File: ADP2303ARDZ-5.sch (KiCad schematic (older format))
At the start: 11 parts

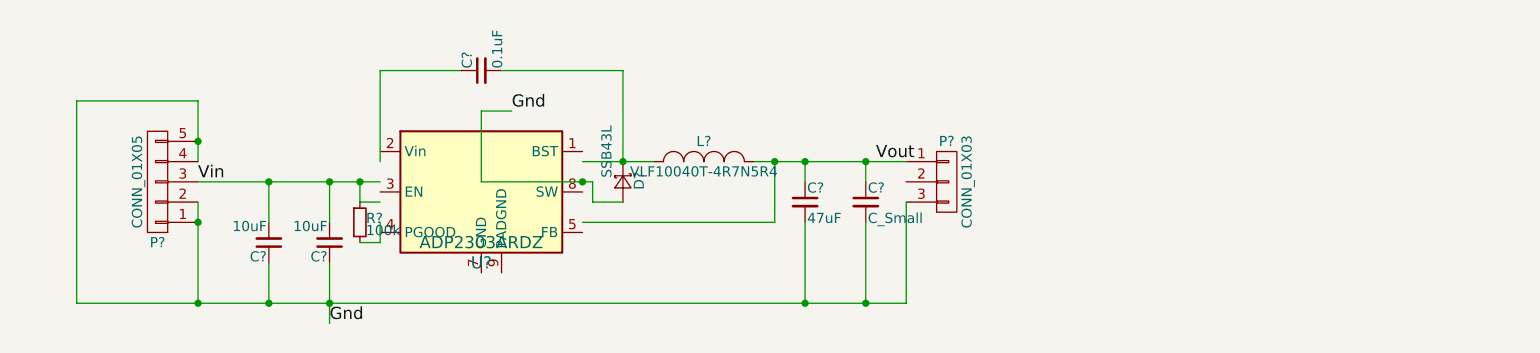
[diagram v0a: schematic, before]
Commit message: Created the board file but not laid out as yet.
Signed-off-by: John Whitmore <johnfwhitmore@gmail.com>
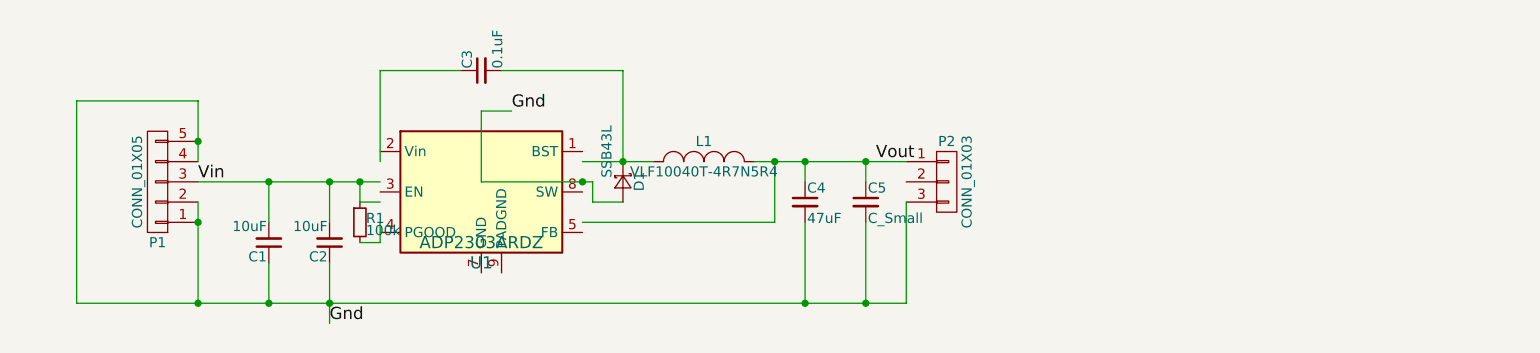
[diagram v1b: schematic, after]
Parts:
- C1, C2, C3, C4, C5: renamed from C?; footprint (none) -> Capacitors_SMD:C_0603_HandSoldering
- D1: renamed from D?; footprint (none) -> Diodes_SMD:DO-214AB_Handsoldering
- L1: renamed from L?; footprint (none) -> electronicSoup:VLF10040_Inductor
- P1: renamed from P?; footprint (none) -> Pin_Headers:Pin_Header_Straight_1x05
- P2: renamed from P?; footprint (none) -> Pin_Headers:Pin_Header_Straight_1x03
- R1: renamed from R?; footprint (none) -> Resistors_SMD:R_0603_HandSoldering
- U1: renamed from U?; footprint (none) -> SMD_Packages:SOIC-8-N
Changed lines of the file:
@@
 $EndDescr
 $Comp
-L ADP2303ARDZ U?
+L ADP2303ARDZ U1
 U 1 1 59F0DD7C
 P 5700 3600
-F 0 "U?" H 5700 3250 60  0000 C CNN
+F 0 "U1" H 5700 3250 60  0000 C CNN
 F 1 "ADP2303ARDZ" H 5700 3350 60  0000 C CNN
-F 2 "" H 5700 3600 60  0000 C CNN
+F 2 "SMD_Packages:SOIC-8-N" H 5700 3600 60  0001 C CNN
 F 3 "" H 5700 3600 60  0000 C CNN
 	1    5700 3600
@@
 $EndComp
 $Comp
-L C_Small C?
+L C_Small C2
 U 1 1 59F0DDA1
 P 4950 3850
-F 0 "C?" H 4960 3920 50  0000 L CNN
+F 0 "C2" H 4960 3920 50  0000 L CNN
 F 1 "10uF" H 4960 3770 50  0000 L CNN
-F 2 "" H 4950 3850 50  0000 C CNN
+F 2 "Capacitors_SMD:C_0603_HandSoldering" H 4950 3850 50  0001 C CNN
 F 3 "" H 4950 3850 50  0000 C CNN
 	1    4950 3850
@@
 $EndComp
 $Comp
-L C_Small C?
+L C_Small C4
 U 1 1 59F0DE2E
 P 7300 3650
-F 0 "C?" H 7310 3720 50  0000 L CNN
+F 0 "C4" H 7310 3720 50  0000 L CNN
 F 1 "47uF" H 7310 3570 50  0000 L CNN
-F 2 "" H 7300 3650 50  0000 C CNN
+F 2 "Capacitors_SMD:C_0603_HandSoldering" H 7300 3650 50  0001 C CNN
 F 3 "" H 7300 3650 50  0000 C CNN
 	1    7300 3650
@@
 $EndComp
 $Comp
-L C_Small C?
+L C_Small C3
 U 1 1 59F0DF1E
 P 5700 3000
-F 0 "C?" H 5710 3070 50  0000 L CNN
+F 0 "C3" H 5710 3070 50  0000 L CNN
 F 1 "0.1uF" H 5710 2920 50  0000 L CNN
-F 2 "" H 5700 3000 50  0000 C CNN
+F 2 "Capacitors_SMD:C_0603_HandSoldering" H 5700 3000 50  0001 C CNN
 F 3 "" H 5700 3000 50  0000 C CNN
 	1    5700 3000
@@
 Gnd
 $Comp
-L D_Schottky_Small D?
+L D_Schottky_Small D1
 U 1 1 59F0DF9A
 P 6400 3550
-F 0 "D?" H 6350 3630 50  0000 L CNN
+F 0 "D1" H 6350 3630 50  0000 L CNN
 F 1 "SSB43L" H 6120 3470 50  0000 L CNN
-F 2 "" V 6400 3550 50  0000 C CNN
+F 2 "Diodes_SMD:DO-214AB_Handsoldering" V 6400 3550 50  0001 C CNN
 F 3 "" V 6400 3550 50  0000 C CNN
 	1    6400 3550
@@
 	6200 3450 6550 3450
 $Comp
-L INDUCTOR_SMALL L?
+L INDUCTOR_SMALL L1
 U 1 1 59F0E044
 P 6800 3450
-F 0 "L?" H 6800 3550 50  0000 C CNN
+F 0 "L1" H 6800 3550 50  0000 C CNN
 F 1 "VLF10040T-4R7N5R4" H 6800 3400 50  0000 C CNN
-F 2 "" H 6800 3450 50  0000 C CNN
+F 2 "electronicSoup:VLF10040_Inductor" H 6800 3450 50  0001 C CNN
 F 3 "" H 6800 3450 50  0000 C CNN
 	1    6800 3450
@@
 Vout
 $Comp
-L CONN_01X05 P?
+L CONN_01X05 P1
 U 1 1 59F0E19C
 P 4100 3550
-F 0 "P?" H 4100 3850 50  0000 C CNN
+F 0 "P1" H 4100 3850 50  0000 C CNN
 F 1 "CONN_01X05" V 4200 3550 50  0000 C CNN
-F 2 "" H 4100 3550 50  0000 C CNN
+F 2 "Pin_Headers:Pin_Header_Straight_1x05" H 4100 3550 50  0001 C CNN
 F 3 "" H 4100 3550 50  0000 C CNN
 	1    4100 3550
@@
 Connection ~ 4300 3350
 $Comp
-L CONN_01X03 P?
+L CONN_01X03 P2
 U 1 1 59F0E2CF
 P 8000 3550
-F 0 "P?" H 8000 3750 50  0000 C CNN
+F 0 "P2" H 8000 3750 50  0000 C CNN
 F 1 "CONN_01X03" V 8100 3550 50  0000 C CNN
-F 2 "" H 8000 3550 50  0000 C CNN
+F 2 "Pin_Headers:Pin_Header_Straight_1x03" H 8000 3550 50  0001 C CNN
 F 3 "" H 8000 3550 50  0000 C CNN
 	1    8000 3550
@@
 Connection ~ 7300 4150
 $Comp
-L R_Small R?
+L R_Small R1
 U 1 1 59F0E3EF
 P 5100 3750
-F 0 "R?" H 5130 3770 50  0000 L CNN
+F 0 "R1" H 5130 3770 50  0000 L CNN
 F 1 "100k" H 5130 3710 50  0000 L CNN
-F 2 "" H 5100 3750 50  0000 C CNN
+F 2 "Resistors_SMD:R_0603_HandSoldering" H 5100 3750 50  0001 C CNN
 F 3 "" H 5100 3750 50  0000 C CNN
 	1    5100 3750
@@
 	5200 3850 5200 3750
 $Comp
-L C_Small C?
+L C_Small C5
 U 1 1 59F0E60C
 P 7600 3650
-F 0 "C?" H 7610 3720 50  0000 L CNN
+F 0 "C5" H 7610 3720 50  0000 L CNN
 F 1 "C_Small" H 7610 3570 50  0000 L CNN
-F 2 "" H 7600 3650 50  0000 C CNN
+F 2 "Capacitors_SMD:C_0603_HandSoldering" H 7600 3650 50  0001 C CNN
 F 3 "" H 7600 3650 50  0000 C CNN
 	1    7600 3650
@@
 Connection ~ 4950 3550
 $Comp
-L C_Small C?
+L C_Small C1
 U 1 1 59F0E819
 P 4650 3850
-F 0 "C?" H 4660 3920 50  0000 L CNN
+F 0 "C1" H 4660 3920 50  0000 L CNN
 F 1 "10uF" H 4660 3770 50  0000 L CNN
-F 2 "" H 4650 3850 50  0000 C CNN
+F 2 "Capacitors_SMD:C_0603_HandSoldering" H 4650 3850 50  0001 C CNN
 F 3 "" H 4650 3850 50  0000 C CNN
 	1    4650 3850

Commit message: Added the dc-dc converters to the official kicad library
Forked the kicad-libraries github project and added the ADP230x and MCP1825s and used both components in this design
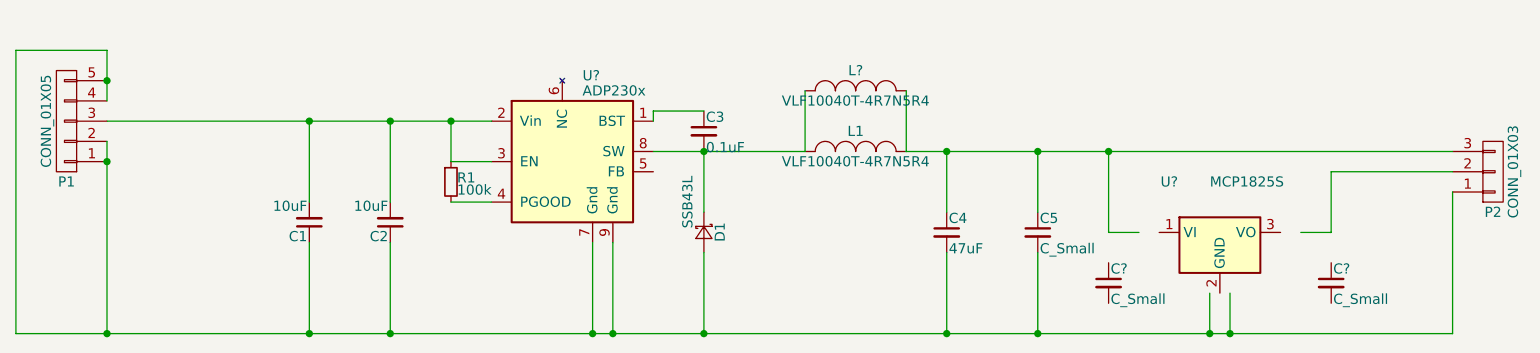
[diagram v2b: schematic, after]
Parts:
- removed U1: ADP2303ARDZ, SMD_Packages:SOIC-8-N, symbol ADP2303ARDZ
- added C? (x2): C_Small, Capacitors_SMD:C_0603_HandSoldering, symbol C_Small
- added L?: VLF10040T-4R7N5R4, electronicSoup:VLF10040_Inductor, symbol INDUCTOR_SMALL
- added U?: ADP230x, Housings_SOIC:SOIC-8-1EP_3.9x4.9mm_Pitch1.27mm, symbol ADP230x
- added U?: MCP1825S, TO_SOT_Packages_SMD:SOT-223, symbol MCP1825S
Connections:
- net labels removed: Gnd, Vin, Vout
- wire segments 32 -> 35
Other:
- moved on the sheet: C1, C2, C3, C4, C5, D1, L1, P1, P2, R1

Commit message: moved to v5 footprints so a few missing
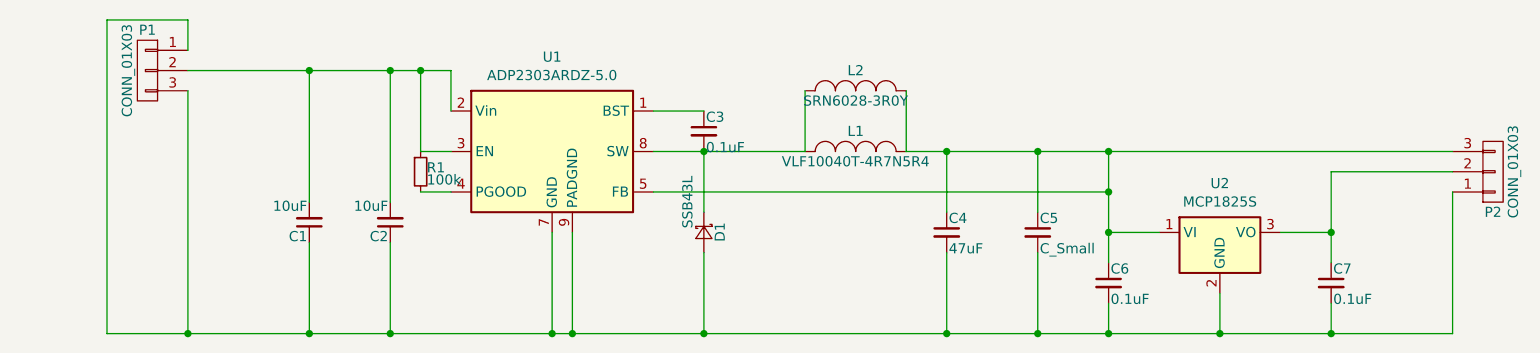
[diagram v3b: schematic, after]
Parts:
- removed P1: CONN_01X05, Pin_Headers:Pin_Header_Straight_1x05, symbol CONN_01X05
- removed U?: ADP230x, Housings_SOIC:SOIC-8-1EP_3.9x4.9mm_Pitch1.27mm, symbol ADP230x
- removed U?: MCP1825S, TO_SOT_Packages_SMD:SOT-223, symbol MCP1825S
- added P1: CONN_01X03, Conn_PinSocket_2.54mm:PinSocket_1x03_P2.54mm_Vertical, symbol CONN_01X03
- added U1: ADP2303ARDZ-5.0, Housings_SOIC:SOIC-8-1EP_3.9x4.9mm_Pitch1.27mm, symbol ADP2303ARDZ-5.0
- added U2: MCP1825S, symbol MCP1825S
- C1, C2, C3, C4, C5: footprint Capacitors_SMD:C_0603_HandSoldering -> Capacitor_SMD:C_0603_1608Metric_Pad0.84x1.00mm_HandSolder
- C6, C7: renamed from C?; value C_Small -> 0.1uF; footprint Capacitors_SMD:C_0603_HandSoldering -> Capacitor_SMD:C_0603_1608Metric_Pad0.84x1.00mm_HandSolder
- D1: footprint Diodes_SMD:DO-214AB_Handsoldering -> Diode_SMD:D_SMB_Handsoldering
- L1: footprint electronicSoup:VLF10040_Inductor -> Inductor_SMD:L_TDK_VLF10040
- L2: renamed from L?; value VLF10040T-4R7N5R4 -> SRN6028-3R0Y; footprint electronicSoup:VLF10040_Inductor -> Inductor_SMD:L_Bourns-SRN6028
- P2: footprint Pin_Headers:Pin_Header_Straight_1x03 -> Conn_PinSocket_2.54mm:PinSocket_1x03_P2.54mm_Vertical
- R1: footprint Resistors_SMD:R_0603_HandSoldering -> Resistor_SMD:R_0603_1608Metric_Pad0.84x1.00mm_HandSolder
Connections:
- wire segments 35 -> 37
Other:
- moved on the sheet: R1
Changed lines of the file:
@@
-EESchema Schematic File Version 2
+EESchema Schematic File Version 3
+LIBS:ADP2303ARDZ-5-rescue
 LIBS:ac-dc
 LIBS:adc-dac
@@
 LIBS:Zilog
 LIBS:ADP2303ARDZ-5-cache
-EELAYER 25 0
+EELAYER 26 0
 EELAYER END
 $Descr A4 11693 8268
@@
 F 0 "C2" H 5260 3820 50  0000 L CNN
 F 1 "10uF" H 5260 3670 50  0000 L CNN
-F 2 "Capacitors_SMD:C_0603_HandSoldering" H 5250 3750 50  0001 C CNN
+F 2 "Capacitor_SMD:C_0603_1608Metric_Pad0.84x1.00mm_HandSolder" H 5250 3750 50  0001 C CNN
 F 3 "" H 5250 3750 50  0000 C CNN
 	1    5250 3750
@@
 F 0 "C4" H 8010 3870 50  0000 L CNN
 F 1 "47uF" H 8010 3720 50  0000 L CNN
-F 2 "Capacitors_SMD:C_0603_HandSoldering" H 8000 3800 50  0001 C CNN
+F 2 "Capacitor_SMD:C_0603_1608Metric_Pad0.84x1.00mm_HandSolder" H 8000 3800 50  0001 C CNN
 F 3 "" H 8000 3800 50  0000 C CNN
 	1    8000 3800
@@
 F 0 "C3" H 6810 3370 50  0000 L CNN
 F 1 "0.1uF" H 6810 3220 50  0000 L CNN
-F 2 "Capacitors_SMD:C_0603_HandSoldering" H 6800 3300 50  0001 C CNN
+F 2 "Capacitor_SMD:C_0603_1608Metric_Pad0.84x1.00mm_HandSolder" H 6800 3300 50  0001 C CNN
 F 3 "" H 6800 3300 50  0000 C CNN
 	1    6800 3300
@@
 F 0 "D1" H 6750 3880 50  0000 L CNN
 F 1 "SSB43L" H 6520 3720 50  0000 L CNN
-F 2 "Diodes_SMD:DO-214AB_Handsoldering" V 6800 3800 50  0001 C CNN
+F 2 "Diode_SMD:D_SMB_Handsoldering" V 6800 3800 50  0001 C CNN
 F 3 "" V 6800 3800 50  0000 C CNN
 	1    6800 3800
@@
 F 0 "L1" H 7550 3500 50  0000 C CNN
 F 1 "VLF10040T-4R7N5R4" H 7550 3350 50  0000 C CNN
-F 2 "electronicSoup:VLF10040_Inductor" H 7550 3400 50  0001 C CNN
+F 2 "Inductor_SMD:L_TDK_VLF10040" H 7550 3400 50  0001 C CNN
 F 3 "" H 7550 3400 50  0000 C CNN
 	1    7550 3400
 	1    0    0    -1
-$EndComp
-$Comp
-L CONN_01X05 P1
-U 1 1 59F0E19C
-P 3650 3250
-F 0 "P1" H 3650 3550 50  0000 C CNN
-F 1 "CONN_01X05" V 3750 3250 50  0000 C CNN
-F 2 "Pin_Headers:Pin_Header_Straight_1x05" H 3650 3250 50  0001 C CNN
-F 3 "" H 3650 3250 50  0000 C CNN
-	1    3650 3250
-	-1   0    0    1
 $EndComp
 $Comp
@@
 F 0 "P2" H 10700 3700 50  0000 C CNN
 F 1 "CONN_01X03" V 10800 3500 50  0000 C CNN
-F 2 "Pin_Headers:Pin_Header_Straight_1x03" H 10700 3500 50  0001 C CNN
+F 2 "Conn_PinSocket_2.54mm:PinSocket_1x03_P2.54mm_Vertical" H 10700 3500 50  0001 C CNN
 F 3 "" H 10700 3500 50  0000 C CNN
 	1    10700 3500
@@
 L R_Small R1
 U 1 1 59F0E3EF
-P 5550 3550
-F 0 "R1" H 5580 3570 50  0000 L CNN
-F 1 "100k" H 5580 3510 50  0000 L CNN
-F 2 "Resistors_SMD:R_0603_HandSoldering" H 5550 3550 50  0001 C CNN
-F 3 "" H 5550 3550 50  0000 C CNN
-	1    5550 3550
+P 5400 3500
+F 0 "R1" H 5430 3520 50  0000 L CNN
+F 1 "100k" H 5430 3460 50  0000 L CNN
+F 2 "Resistor_SMD:R_0603_1608Metric_Pad0.84x1.00mm_HandSolder" H 5400 3500 50  0001 C CNN
+F 3 "" H 5400 3500 50  0000 C CNN
+	1    5400 3500
 	1    0    0    -1
 $EndComp
@@
 F 0 "C5" H 8460 3870 50  0000 L CNN
 F 1 "C_Small" H 8460 3720 50  0000 L CNN
-F 2 "Capacitors_SMD:C_0603_HandSoldering" H 8450 3800 50  0001 C CNN
+F 2 "Capacitor_SMD:C_0603_1608Metric_Pad0.84x1.00mm_HandSolder" H 8450 3800 50  0001 C CNN
 F 3 "" H 8450 3800 50  0000 C CNN
 	1    8450 3800
@@
 F 0 "C1" H 4860 3820 50  0000 L CNN
 F 1 "10uF" H 4860 3670 50  0000 L CNN
-F 2 "Capacitors_SMD:C_0603_HandSoldering" H 4850 3750 50  0001 C CNN
+F 2 "Capacitor_SMD:C_0603_1608Metric_Pad0.84x1.00mm_HandSolder" H 4850 3750 50  0001 C CNN
 F 3 "" H 4850 3750 50  0000 C CNN
 	1    4850 3750
 	-1   0    0    1
 $EndComp
-$Comp
-L ADP230x U?
-U 1 1 59F6EFDE
-P 6150 3450
-F 0 "U?" H 6200 3875 50  0000 L CNN
-F 1 "ADP230x" H 6200 3800 50  0000 L CNN
-F 2 "Housings_SOIC:SOIC-8-1EP_3.9x4.9mm_Pitch1.27mm" H 6200 3100 50  0001 L CNN
-F 3 "" H 5950 4050 50  0001 C CNN
-	1    6150 3450
-	1    0    0    -1
-$EndComp
-Wire Wire Line
-	5750 3650 5550 3650
-Wire Wire Line
-	5750 3450 5550 3450
-Wire Wire Line
-	3850 3250 5750 3250
-Wire Wire Line
-	4850 3650 4850 3250
-Connection ~ 4850 3250
-Wire Wire Line
-	5250 3650 5250 3250
-Connection ~ 5250 3250
-Wire Wire Line
-	5550 3450 5550 3250
-Connection ~ 5550 3250
-Wire Wire Line
-	3850 2900 3850 3150
-Wire Wire Line
-	3850 2900 3400 2900
-Wire Wire Line
-	3400 2900 3400 4300
-Wire Wire Line
-	3400 4300 10500 4300
-Wire Wire Line
-	6350 4300 6350 3850
-Connection ~ 3850 3050
-Wire Wire Line
-	6250 3850 6250 4300
-Connection ~ 6250 4300
-Wire Wire Line
-	3850 3350 3850 4300
-Connection ~ 3850 4300
-Connection ~ 3850 3450
-Wire Wire Line
-	4850 3850 4850 4300
+Wire Wire Line
+	4850 3000 4850 3650
+Wire Wire Line
+	5250 3000 5250 3650
+Wire Wire Line
+	4850 4300 4850 3850
 Connection ~ 4850 4300
 Wire Wire Line
-	5250 3850 5250 4300
+	5250 4300 5250 3850
 Connection ~ 5250 4300
 Wire Wire Line
@@
 Wire Wire Line
 	6800 3200 6550 3200
-Wire Wire Line
-	6550 3200 6550 3250
-$Comp
-L INDUCTOR_SMALL L?
+$Comp
+L INDUCTOR_SMALL L2
 U 1 1 59F6F8C3
 P 7550 3100
-F 0 "L?" H 7550 3200 50  0000 C CNN
-F 1 "VLF10040T-4R7N5R4" H 7550 3050 50  0000 C CNN
-F 2 "electronicSoup:VLF10040_Inductor" H 7550 3100 50  0001 C CNN
+F 0 "L2" H 7550 3200 50  0000 C CNN
+F 1 "SRN6028-3R0Y" H 7550 3050 50  0000 C CNN
+F 2 "Inductor_SMD:L_Bourns-SRN6028" H 7550 3100 50  0001 C CNN
 F 3 "" H 7550 3100 50  0000 C CNN
 	1    7550 3100
@@
 Wire Wire Line
 	6800 3700 6800 3400
-Connection ~ 6350 4300
-Wire Wire Line
-	6800 3900 6800 4300
+Wire Wire Line
+	6800 4300 6800 3900
 Connection ~ 6800 4300
 Wire Wire Line
-	8000 3900 8000 4300
+	8000 4300 8000 3900
 Connection ~ 8000 4300
 Wire Wire Line
-	8450 3900 8450 4300
+	8450 4300 8450 3900
 Connection ~ 8450 4300
-$Comp
-L MCP1825S U?
-U 1 1 59F71C5D
-P 9350 3800
-F 0 "U?" H 9100 4050 50  0000 C CNN
-F 1 "MCP1825S" H 9300 4050 50  0000 L CNN
-F 2 "TO_SOT_Packages_SMD:SOT-223" H 9400 3550 50  0001 L CNN
-F 3 "" H 9350 3300 50  0001 C CNN
-	1    9350 3800
-	1    0    0    -1
-$EndComp
-Wire Wire Line
-	9300 4300 9300 4100
 Wire Wire Line
 	10500 4300 10500 3600
-Connection ~ 9300 4300
-Wire Wire Line
-	9400 4100 9400 4300
-Connection ~ 9400 4300
-Wire Wire Line
-	8950 3800 8800 3800
-Wire Wire Line
-	8800 3800 8800 3400
+Wire Wire Line
+	8800 3800 9050 3800
+Wire Wire Line
+	8800 3400 8800 3950
 Connection ~ 8800 3400
 Wire Wire Line
@@
 Connection ~ 8000 3400
 Wire Wire Line
-	9900 3800 9750 3800
-Wire Wire Line
-	9900 3500 9900 3800
+	9650 3800 9900 3800
+Wire Wire Line
+	9900 3500 9900 3950
 Wire Wire Line
 	9900 3500 10500 3500
 $Comp
-L C_Small C?
+L C_Small C6
 U 1 1 59F722DC
 P 8800 4050
-F 0 "C?" H 8810 4120 50  0000 L CNN
-F 1 "C_Small" H 8810 3970 50  0000 L CNN
-F 2 "Capacitors_SMD:C_0603_HandSoldering" H 8800 4050 50  0001 C CNN
+F 0 "C6" H 8810 4120 50  0000 L CNN
+F 1 "0.1uF" H 8810 3970 50  0000 L CNN
+F 2 "Capacitor_SMD:C_0603_1608Metric_Pad0.84x1.00mm_HandSolder" H 8800 4050 50  0001 C CNN
 F 3 "" H 8800 4050 50  0000 C CNN
 	1    8800 4050
@@
 $EndComp
 $Comp
-L C_Small C?
+L C_Small C7
 U 1 1 59F7232E
 P 9900 4050
-F 0 "C?" H 9910 4120 50  0000 L CNN
-F 1 "C_Small" H 9910 3970 50  0000 L CNN
-F 2 "Capacitors_SMD:C_0603_HandSoldering" H 9900 4050 50  0001 C CNN
+F 0 "C7" H 9910 4120 50  0000 L CNN
+F 1 "0.1uF" H 9910 3970 50  0000 L CNN
+F 2 "Capacitor_SMD:C_0603_1608Metric_Pad0.84x1.00mm_HandSolder" H 9900 4050 50  0001 C CNN
 F 3 "" H 9900 4050 50  0000 C CNN
 	1    9900 4050
 	1    0    0    -1
 $EndComp
+Wire Wire Line
+	8800 4300 8800 4150
+Connection ~ 8800 4300
+Wire Wire Line
+	9900 4300 9900 4150
+Connection ~ 9900 4300
+Connection ~ 8800 3800
+Connection ~ 9900 3800
+Wire Wire Line
+	6550 3600 8800 3600
+Connection ~ 8800 3600
+Wire Wire Line
+	6050 4300 6050 3800
+Connection ~ 6050 4300
+Wire Wire Line
+	6150 4300 6150 3800
+Connection ~ 6150 4300
+$Comp
+L CONN_01X03 P1
+U 1 1 59F8873E
+P 4050 3000
+F 0 "P1" H 4050 3200 50  0000 C CNN
+F 1 "CONN_01X03" V 4150 3000 50  0000 C CNN
+F 2 "Conn_PinSocket_2.54mm:PinSocket_1x03_P2.54mm_Vertical" H 4050 3000 50  0001 C CNN
+F 3 "" H 4050 3000 50  0000 C CNN
+	1    4050 3000
+	-1   0    0    -1
+$EndComp
+Connection ~ 4850 3000
+Connection ~ 5250 3000
+Wire Wire Line
+	4250 3100 4250 4300
+Connection ~ 4250 4300
+Wire Wire Line
+	4250 2900 4250 2750
+Wire Wire Line
+	4250 2750 3850 2750
+Wire Wire Line
+	3850 2750 3850 4300
+Wire Wire Line
+	3850 4300 10500 4300
+$Comp
+L ADP2303ARDZ-5.0 U1
+U 1 1 5A05A19A
+P 6050 3400
+F 0 "U1" H 6050 3867 50  0000 C CNN
+F 1 "ADP2303ARDZ-5.0" H 6050 3776 50  0000 C CNN
+F 2 "Housings_SOIC:SOIC-8-1EP_3.9x4.9mm_Pitch1.27mm" H 6200 3050 50  0001 L CNN
+F 3 "http://www.analog.com/media/en/technical-documentation/data-sheets/ADP2302_2303.pdf" H 5850 4000 50  0001 C CNN
+	1    6050 3400
+	1    0    0    -1
+$EndComp
+Wire Wire Line
+	4250 3000 5550 3000
+Wire Wire Line
+	5550 3000 5550 3200
+Wire Wire Line
+	5550 3400 5400 3400
+Wire Wire Line
+	5400 3400 5400 3000
+Connection ~ 5400 3000
+Wire Wire Line
+	5550 3600 5400 3600
+$Comp
+L MCP1825S U2
+U 1 1 5A05AC53
+P 9350 3800
+F 0 "U2" H 9350 4042 50  0000 C CNN
+F 1 "MCP1825S" H 9350 3951 50  0000 C CNN
+F 2 "" H 9250 3950 50  0001 C CNN
+F 3 "http://ww1.microchip.com/downloads/en/devicedoc/22056b.pdf" H 9350 4050 50  0001 C CNN
+	1    9350 3800
+	1    0    0    -1
+$EndComp
+Wire Wire Line
+	9350 4100 9350 4300
+Connection ~ 9350 4300
 $EndSCHEMATC

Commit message: Added feedback resistors so adjustable version could be used.
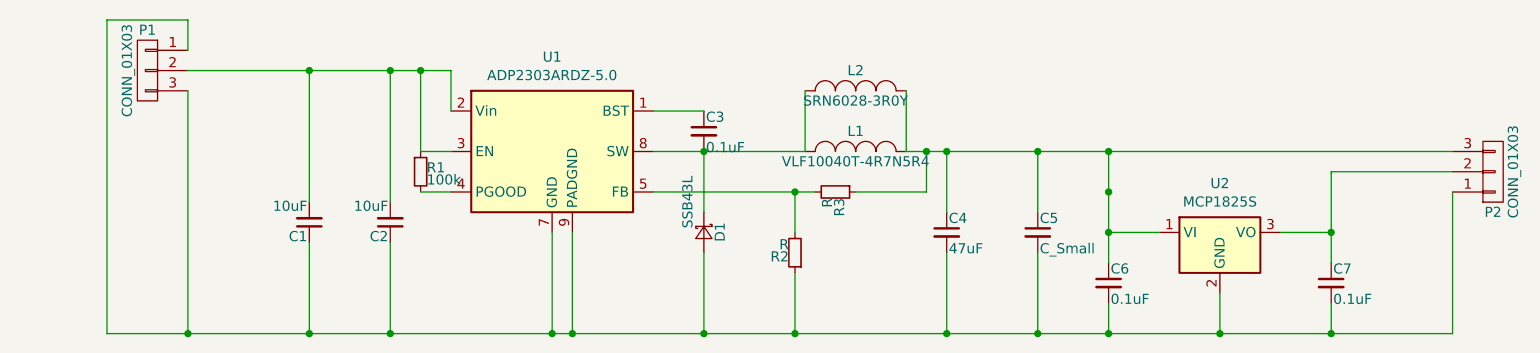
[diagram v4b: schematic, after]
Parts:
- added R2, R3: R, Resistor_SMD:R_0603_1608Metric_Pad0.84x1.00mm_HandSolder, symbol R_Small
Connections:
- net at C1.1, C2.1, C4.2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: now also R2.1
- net at C4.1, C5.1, C6.1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: now also R3.1; no longer U1.5 (FB)
- new net: R2.2, R3.2, U1.5 (FB)
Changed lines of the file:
@@
 Connection ~ 8800 3800
 Connection ~ 9900 3800
-Wire Wire Line
-	6550 3600 8800 3600
 Connection ~ 8800 3600
 Wire Wire Line
@@
 	9350 4100 9350 4300
 Connection ~ 9350 4300
+$Comp
+L R_Small R3
+U 1 1 5A06E760
+P 7450 3600
+F 0 "R3" H 7480 3620 50  0000 L CNN
+F 1 "R" H 7480 3560 50  0000 L CNN
+F 2 "Resistor_SMD:R_0603_1608Metric_Pad0.84x1.00mm_HandSolder" H 7450 3600 50  0001 C CNN
+F 3 "" H 7450 3600 50  0000 C CNN
+	1    7450 3600
+	0    1    1    0
+$EndComp
+$Comp
+L R_Small R2
+U 1 1 5A06E7E0
+P 7250 3900
+F 0 "R2" H 7280 3920 50  0000 L CNN
+F 1 "R" H 7280 3860 50  0000 L CNN
+F 2 "Resistor_SMD:R_0603_1608Metric_Pad0.84x1.00mm_HandSolder" H 7250 3900 50  0001 C CNN
+F 3 "" H 7250 3900 50  0000 C CNN
+	1    7250 3900
+	-1   0    0    1
+$EndComp
+Wire Wire Line
+	6550 3600 7350 3600
+Wire Wire Line
+	7550 3600 7900 3600
+Wire Wire Line
+	7900 3600 7900 3400
+Connection ~ 7900 3400
+Wire Wire Line
+	7250 3800 7250 3600
+Connection ~ 7250 3600
+Wire Wire Line
+	7250 4000 7250 4300
+Connection ~ 7250 4300
 $EndSCHEMATC
